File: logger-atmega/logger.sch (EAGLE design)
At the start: 28 parts, among them IC1 75176AD, IC2 REG1117, U1 MSP430G2352IPW14

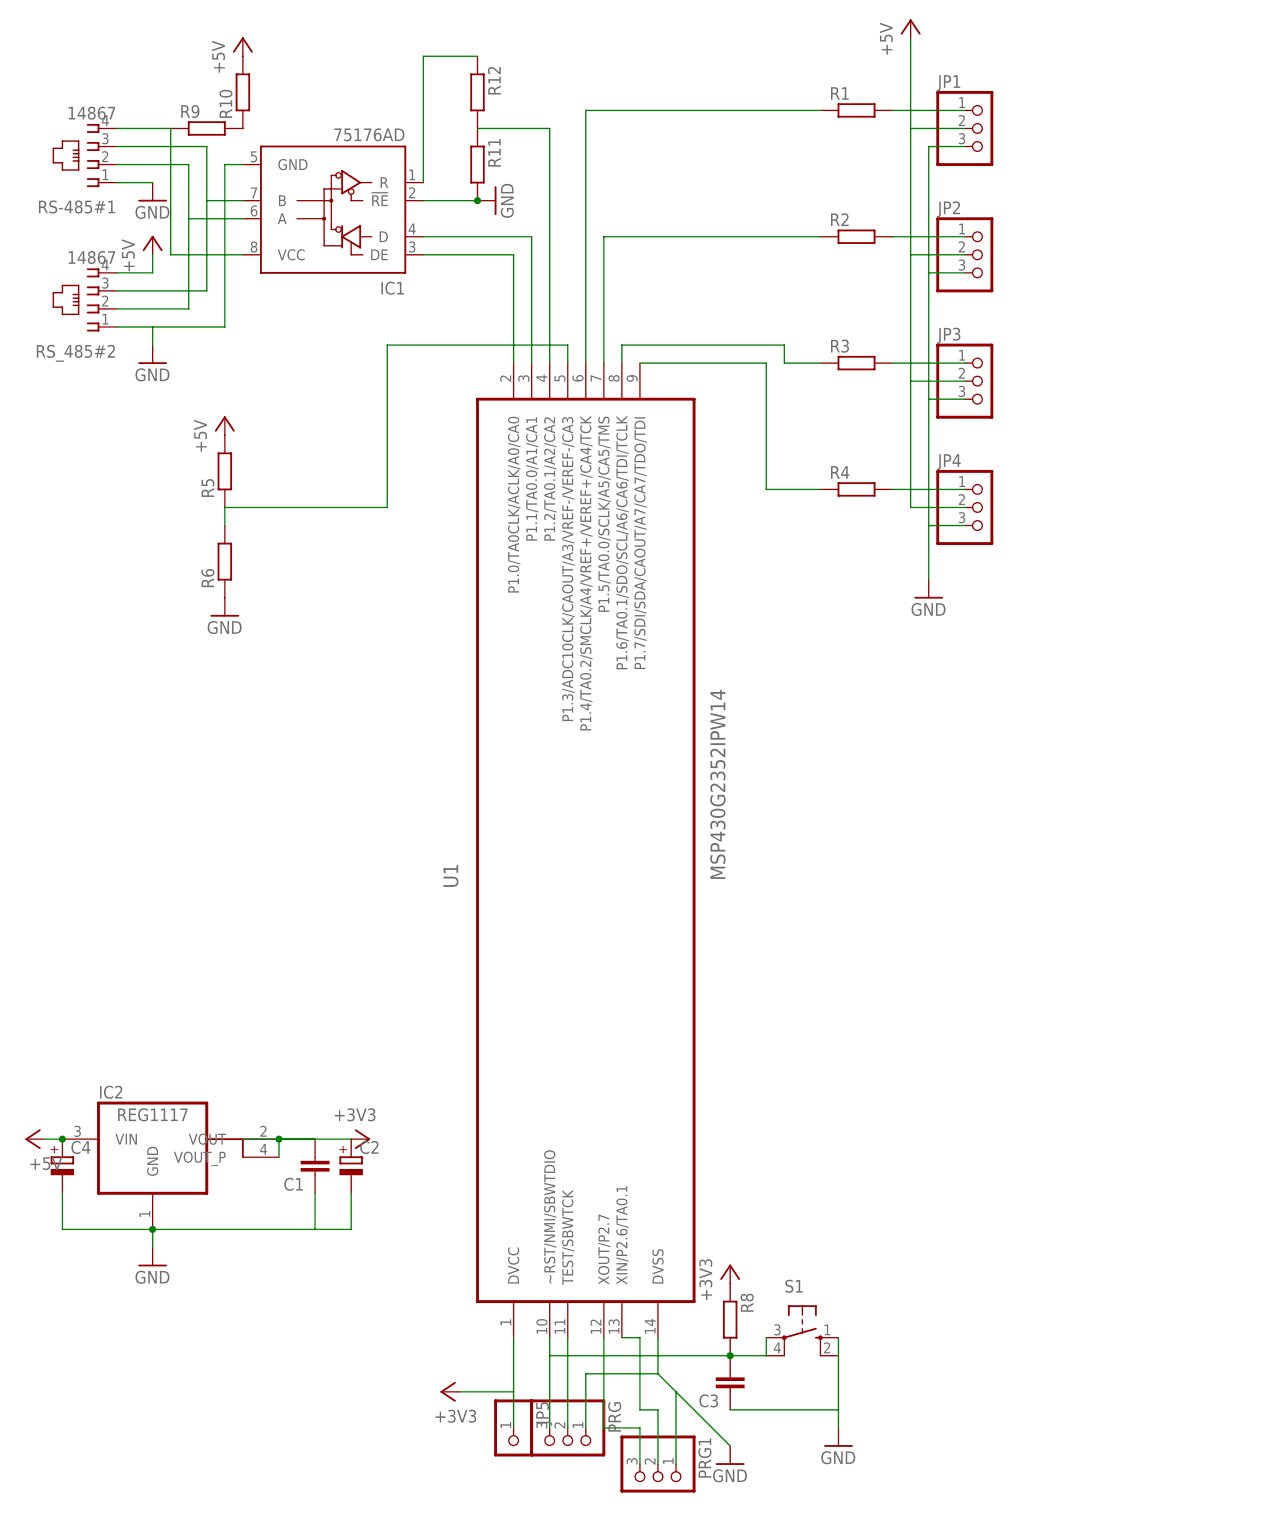
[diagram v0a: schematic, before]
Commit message: ATMega logger routed.
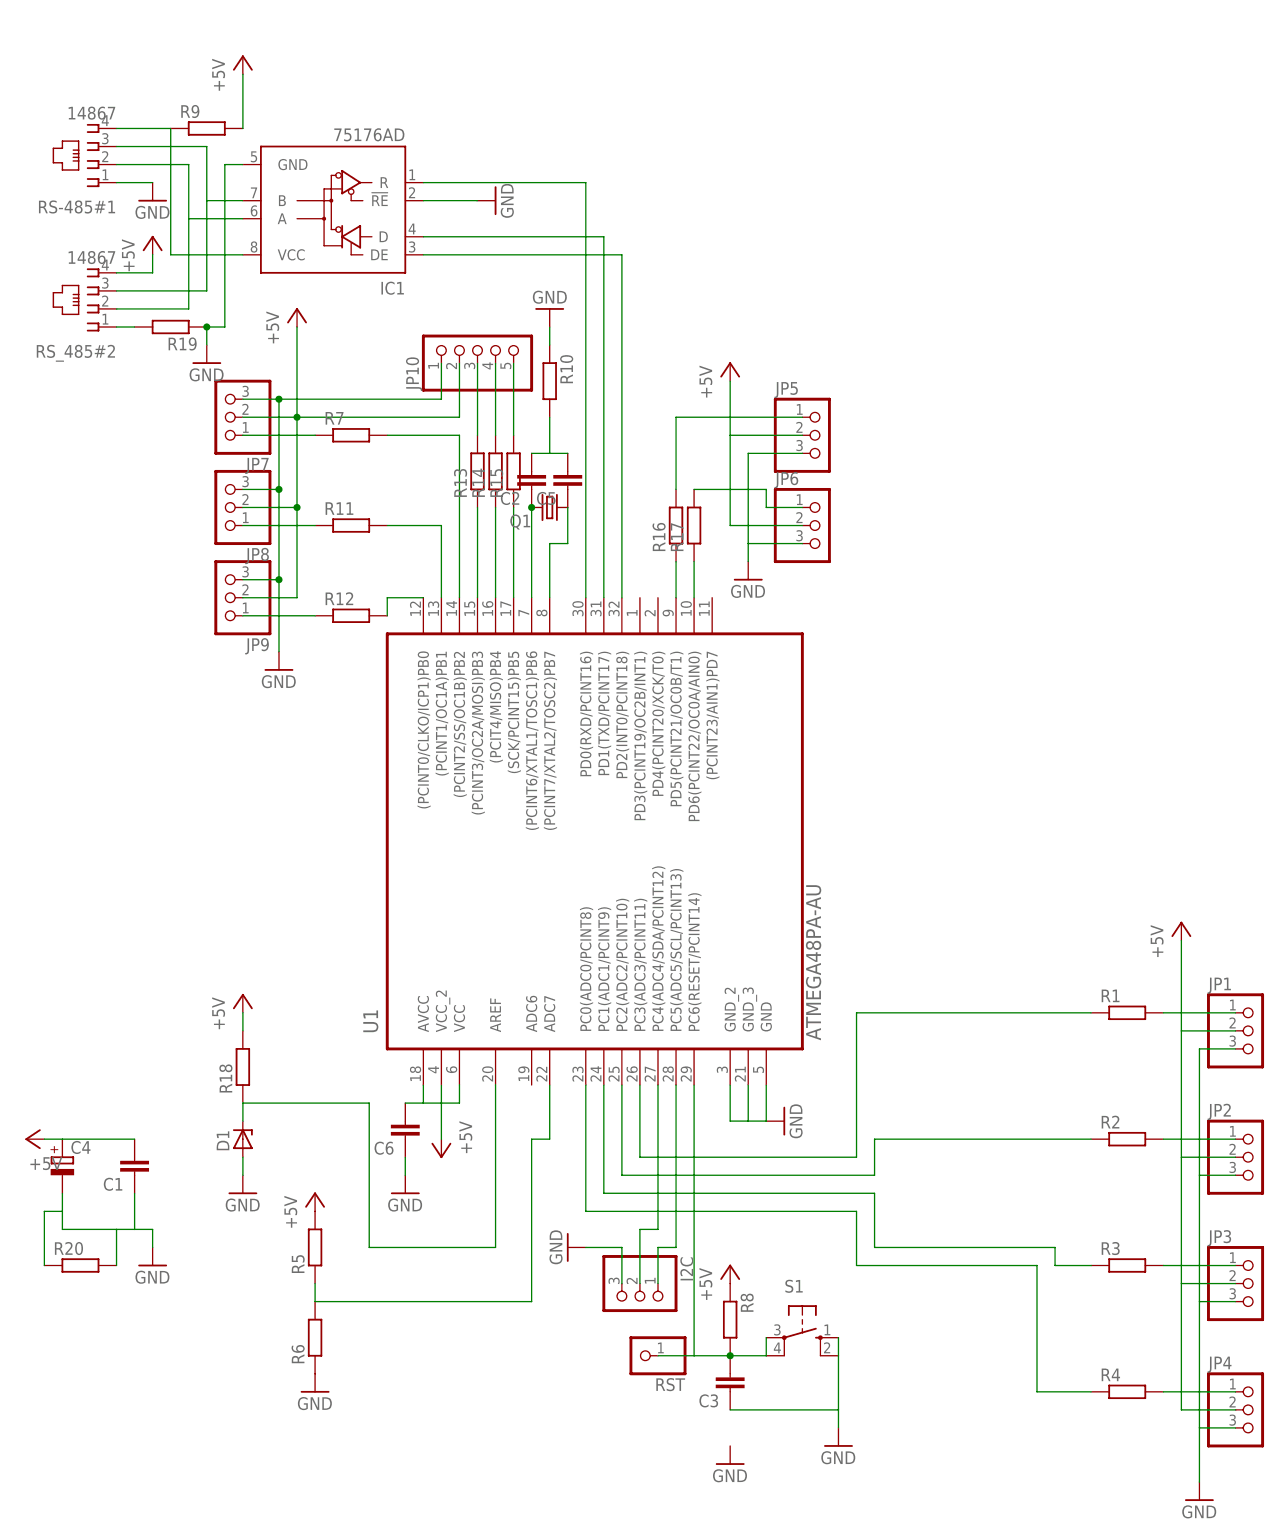
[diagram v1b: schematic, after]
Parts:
- removed IC2: REG1117, burr-brown:REG1117
- removed PRG, PRG1: (no value), pinhead:PINHD-1X3
- added C5, C6: (no value), rcl:C-EUC0805
- added D1: (no value), diode:ZENER-DIODESOD80C
- added I2C, JP6, JP7, JP8, JP9: (no value), pinhead:PINHD-1X3
- added JP10: (no value), pinhead:PINHD-1X5
- added Q1: (no value), crystal:CRYSTALHC49U-V
- added R13, R14, R15, R16, R17, R18, R7: (no value), rcl:R-EU_R0805
- added R19, R20: (no value), rcl:R-EU_R1206
- added RST: (no value), pinhead:PINHD-1X1
- C1: device rcl:C-EUC0805 -> rcl:C-EUC1206
- C2: device rcl:CPOL-EUE2,5-6E -> rcl:C-EUC0805
- JP5: device pinhead:PINHD-1X1 -> pinhead:PINHD-1X3
- R6: device rcl:R-EU_R0805 -> rcl:R-EU_R1206
- U1: value MSP430G2352IPW14 -> ATMEGA48PA-AU; device MSP430G2352IPW14:MSP430G2352IPW14 -> atmega48PA:ATMEGA48PA-AU
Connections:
- removed net +3V3: C1.2, C2.+, IC2.VOUT, IC2.VOUT_P, JP5.1, R8.1, U1.DVCC
- removed net N$19: R10.1, R9.2
- new net DE: IC1.DE, U1.PD2(INT0/PCINT18)
- new net N$17: JP10.3, R13.2
- new net N$23: JP8.1, R11.1
- new net N$24: JP7.1, R7.1
- new net N$25: R13.1, U1.(PCINT3/OC2A/MOSI)PB3
- new net N$26: R14.1, U1.(PCIT4/MISO)PB4
- new net N$27: R16.1, U1.PD5(PCINT21/OC0B/T1)
- new net N$28: R17.1, U1.PD6(PCINT22/OC0A/AIN0)
- new net N$29: R15.1, U1.(SCK/PCINT15)PB5
- new net N$30: R19.2, RS_485#2.1
- new net N$31: R12.2, U1.(PCINT0/CLKO/ICP1)PB0
- new net N$32: R11.2, U1.(PCINT1/OC1A)PB1
- new net N$33: R7.2, U1.(PCINT2/SS/OC1B)PB2
- new net N$34: D1.C, R18.1, U1.AREF
- new net N$35: C2.2, C5.2, R10.2
- new net N$36: JP6.1, R17.2
- new net N$37: JP5.1, R16.2
- new net RX: IC1.R, U1.PD0(RXD/PCINT16)
- new net TX: IC1.D, U1.PD1(TXD/PCINT17)
- net +5V: now also C1.2, C6.2, JP10.2, JP5.2, JP6.2, JP7.2, JP8.2, JP9.2, R18.2, R8.1, R9.2, U1.AVCC, U1.VCC, U1.VCC_2; no longer IC2.VIN, R10.2
- net GND: now also C6.1, D1.A, I2C.3, JP10.1, JP5.3, JP6.3, JP7.3, JP8.3, JP9.3, R10.1, R19.1, R20.1, R20.2, U1.GND, U1.GND_2, U1.GND_3; no longer C2.-, IC2.GND, PRG.1, PRG1.1, R11.2, RS_485#2.1, U1.DVSS
- net N$10: now also U1.PC2(ADC2/PCINT10); no longer U1.P1.5/TA0.0/SCLK/A5/CA5/TMS
- net N$11: now also U1.PC3(ADC3/PCINT11); no longer U1.P1.4/TA0.2/SMCLK/A4/VREF+/VEREF+/CA4/TCK
- net N$12: now also JP9.1, R12.1; no longer PRG1.2, U1.XIN/P2.6/TA0.1
- net N$13: now also JP10.5, R15.2; no longer IC1.D, U1.P1.1/TA0.0/A1/CA1
- net N$14: now also JP10.4, R14.2; no longer IC1.DE, U1.P1.0/TA0CLK/ACLK/A0/CA0
- net N$15: now also RST.1, U1.PC6(RESET/PCINT14); no longer PRG.3, U1.~RST/NMI/SBWTDIO
- net N$16: now also C2.1, Q1.2, U1.(PCINT6/XTAL1/TOSC1)PB6; no longer PRG.2, U1.TEST/SBWTCK
- net N$18: now also C5.1, Q1.1, U1.(PCINT7/XTAL2/TOSC2)PB7; no longer PRG1.3, U1.XOUT/P2.7
- net N$21: now also I2C.1, U1.PC5(ADC5/SCL/PCINT13); no longer IC1.R, R12.1
- net N$22: now also I2C.2, U1.PC4(ADC4/SDA/PCINT12); no longer R11.1, R12.2, U1.P1.2/TA0.1/A2/CA2
- net N$3: now also U1.ADC7; no longer U1.P1.3/ADC10CLK/CAOUT/A3/VREF-/VEREF-/CA3
- net N$4: now also U1.PC0(ADC0/PCINT8); no longer U1.P1.7/SDI/SDA/CAOUT/A7/CA7/TDO/TDI
- net N$9: now also U1.PC1(ADC1/PCINT9); no longer U1.P1.6/TA0.1/SDO/SCL/A6/CA6/TDI/TCLK
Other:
- moved on the sheet: C1, JP1, JP2, JP3, JP4, R1, R10, R11, R12, R2, R3, R4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

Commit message: Upravy desky i schematu, snad definitivni.
Odebrana zenerka, budu verit vnitrni referenci
Pridana civka na analogovou zem
Pridan napajeci konektor

Napajeci cesty rozsireny
Doplneny napisy
Vylito medi
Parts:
- removed D1: (no value), diode:ZENER-DIODESOD80C
- removed R18: (no value), rcl:R-EU_R0805
- added L1: 10uH, rcl:L-EUL1812
- added PWR: (no value), pinhead:PINHD-1X2
- C1: value (none) -> 100n; device rcl:C-EUC1206 -> rcl:C-EUC0805
- C2, C5: value (none) -> 22p
- C6: value (none) -> 100n
- Q1: value (none) -> 10MHz
- R10, R19, R20, R9: value (none) -> 0R
- renumbered JP1 to ADC1, JP10 to SPI, JP2 to ADC2, JP3 to ADC3, JP4 to ADC4, JP5 to PWM3, JP6 to PWM4, JP7 to PWM2, JP8 to PWM1, JP9 to INPUT_PWM
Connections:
- removed net N$34: D1.C, R18.1, U1.AREF
- new net N$19: C1.2, L1.2, U1.AVCC
- net +5V: now also L1.1, PWR.1; no longer C1.2, R18.2, U1.AVCC
- net GND: now also PWR.2; no longer D1.A
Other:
- moved on the sheet: C1, C6

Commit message: Pridan kondenzator na AREF
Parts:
- removed L1: 10uH, rcl:L-EUL1812
- added C7: 100n, rcl:C-EUC0805
- added L2: 10uH, rcl:L-EU
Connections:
- new net N$34: C7.2, U1.AREF
- net +5V: now also L2.1; no longer L1.1
- net GND: now also C7.1
- net N$19: now also L2.2; no longer L1.2
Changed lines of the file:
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@@
 <part name="R20" library="rcl" deviceset="R-EU_" device="R1206" value="0R"/>
 <part name="P+10" library="supply1" deviceset="+5V" device=""/>
-<part name="L1" library="rcl" deviceset="L-EU" device="L1812" value="10uH"/>
 <part name="PWR" library="pinhead" deviceset="PINHD-1X2" device=""/>
+<part name="C7" library="rcl" deviceset="C-EU" device="C0805" value="100n"/>
+<part name="GND15" library="supply1" deviceset="GND" device=""/>
+<part name="L2" library="rcl" deviceset="L-EU" device="" value="10uH"/>
 </parts>
 <sheets>
@@
 <instance part="R20" gate="G$1" x="-10.16" y="-86.36"/>
 <instance part="P+10" gate="1" x="22.86" y="-58.42"/>
-<instance part="L1" gate="G$1" x="27.94" y="-63.5" rot="R90"/>
 <instance part="PWR" gate="G$1" x="7.62" y="-73.66"/>
+<instance part="C7" gate="G$1" x="48.26" y="-68.58" rot="R180"/>
+<instance part="GND15" gate="1" x="48.26" y="-76.2"/>
+<instance part="L2" gate="G$1" x="27.94" y="-63.5" rot="R90"/>
 </instances>
 <busses>
@@
 </segment>
 <segment>
-<pinref part="L1" gate="G$1" pin="1"/>
 <pinref part="P+10" gate="1" pin="+5V"/>
+<pinref part="L2" gate="G$1" pin="1"/>
 <wire x1="22.86" y1="-63.5" x2="22.86" y2="-60.96" width="0.1524" layer="91"/>
 </segment>
@@
 <wire x1="35.56" y1="-71.12" x2="35.56" y2="-73.66" width="0.1524" layer="91"/>
 </segment>
+<segment>
+<pinref part="C7" gate="G$1" pin="1"/>
+<pinref part="GND15" gate="1" pin="GND"/>
+<wire x1="48.26" y1="-71.12" x2="48.26" y2="-73.66" width="0.1524" layer="91"/>
+</segment>
 </net>
 <net name="N$1" class="0">
@@
 <net name="N$19" class="0">
 <segment>
-<pinref part="L1" gate="G$1" pin="2"/>
 <pinref part="C1" gate="G$1" pin="2"/>
 <wire x1="33.02" y1="-63.5" x2="35.56" y2="-63.5" width="0.1524" layer="91"/>
@@
 <wire x1="35.56" y1="-63.5" x2="38.1" y2="-63.5" width="0.1524" layer="91"/>
 <wire x1="38.1" y1="-63.5" x2="38.1" y2="-60.96" width="0.1524" layer="91"/>
-</segment>
-</net>
+<pinref part="L2" gate="G$1" pin="2"/>
+</segment>
+</net>
+<net name="N$34" class="0">
+<segment>
+<pinref part="C7" gate="G$1" pin="2"/>
+<pinref part="U1" gate="A" pin="AREF"/>
+<wire x1="48.26" y1="-63.5" x2="48.26" y2="-60.96" width="0.1524" layer="91"/>
+</segment>
+</net>
